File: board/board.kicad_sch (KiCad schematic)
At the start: 35 parts, among them J1 Conn_01x25_Socket, J2 Conn_01x25_Socket, J5 PJ-320B, J6 Screw_Terminal_01x02, J7 Screw_Terminal_01x02, J8 Screw_Terminal_01x02

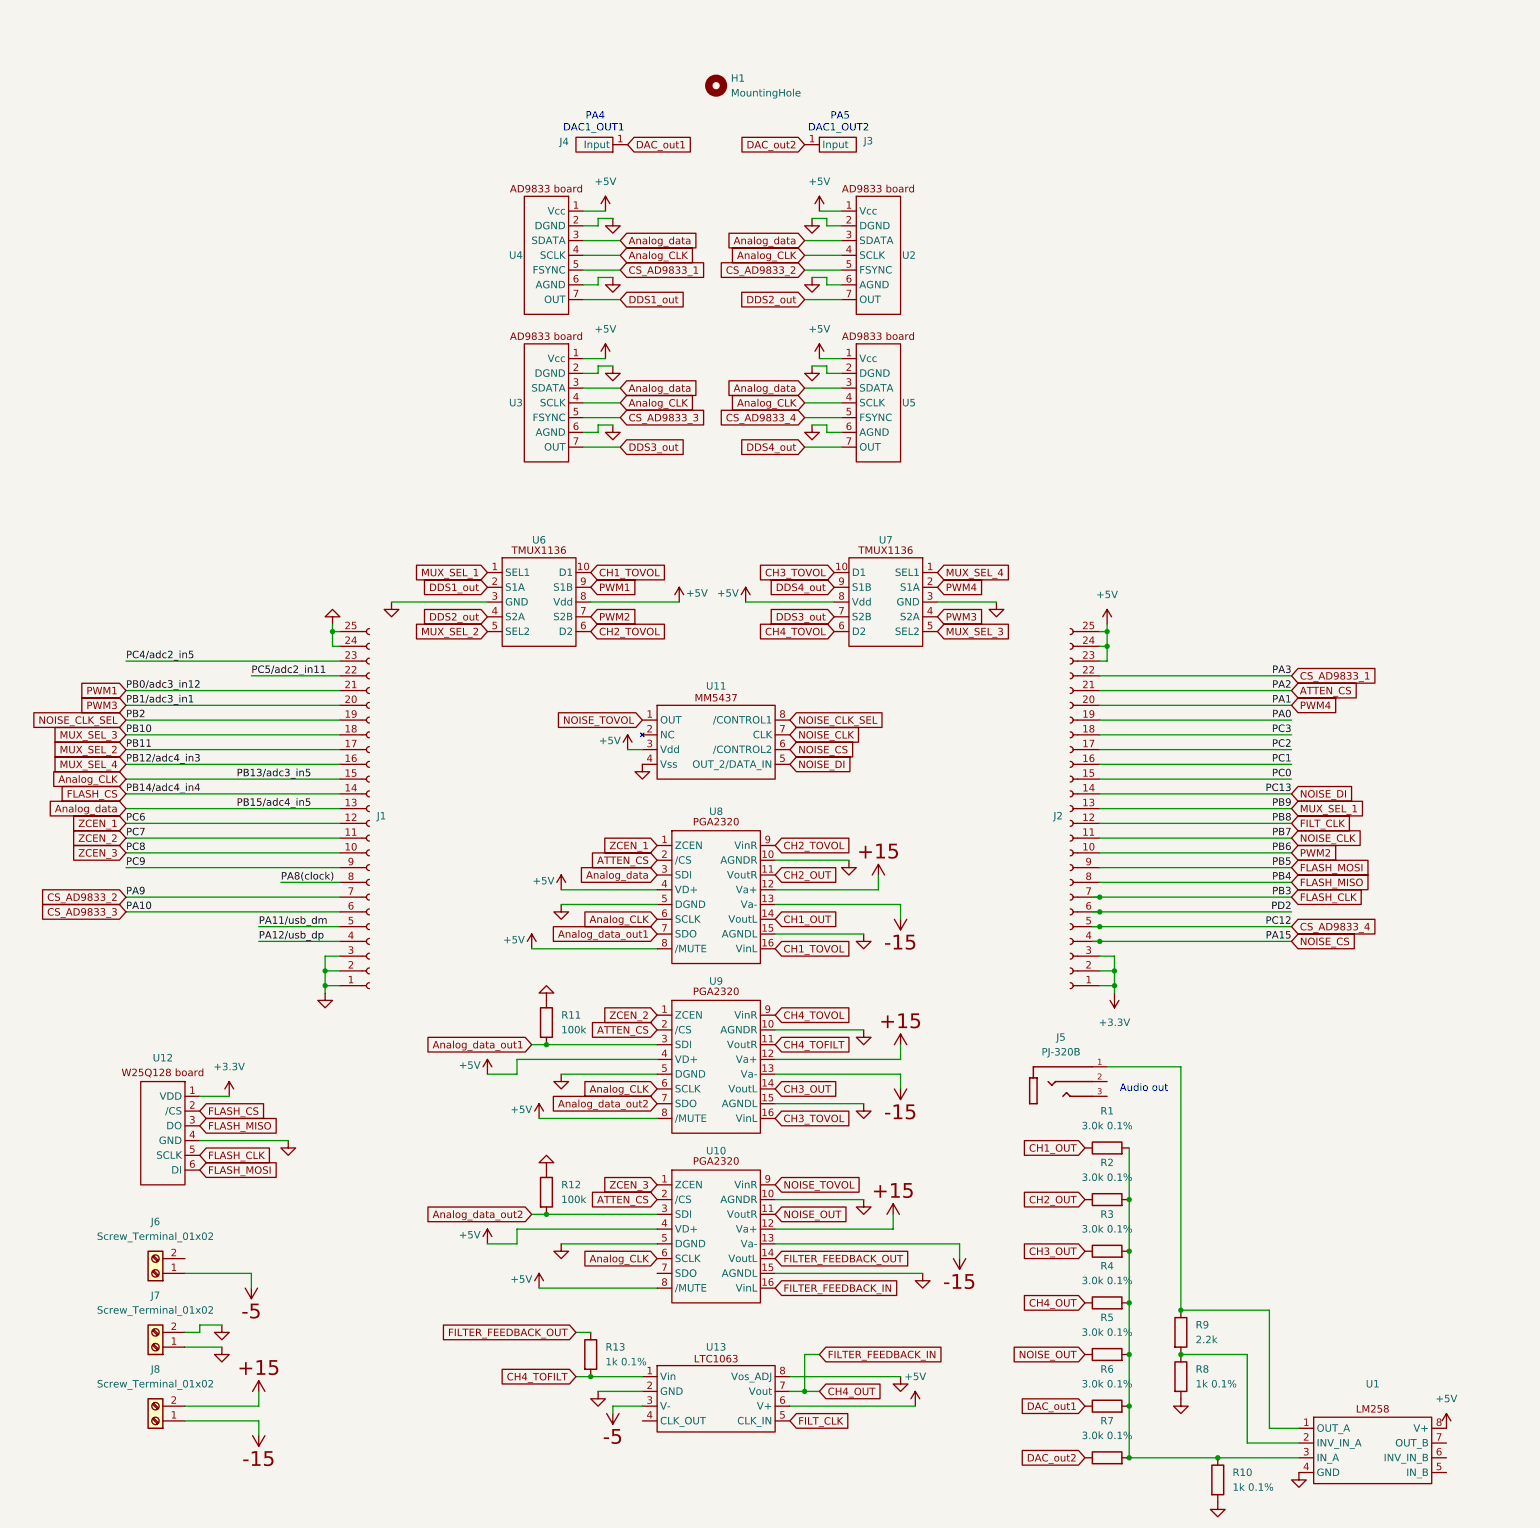
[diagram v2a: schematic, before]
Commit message: fuck it, I ordered 4 2-ch attenuators so let there be DAC volume control!
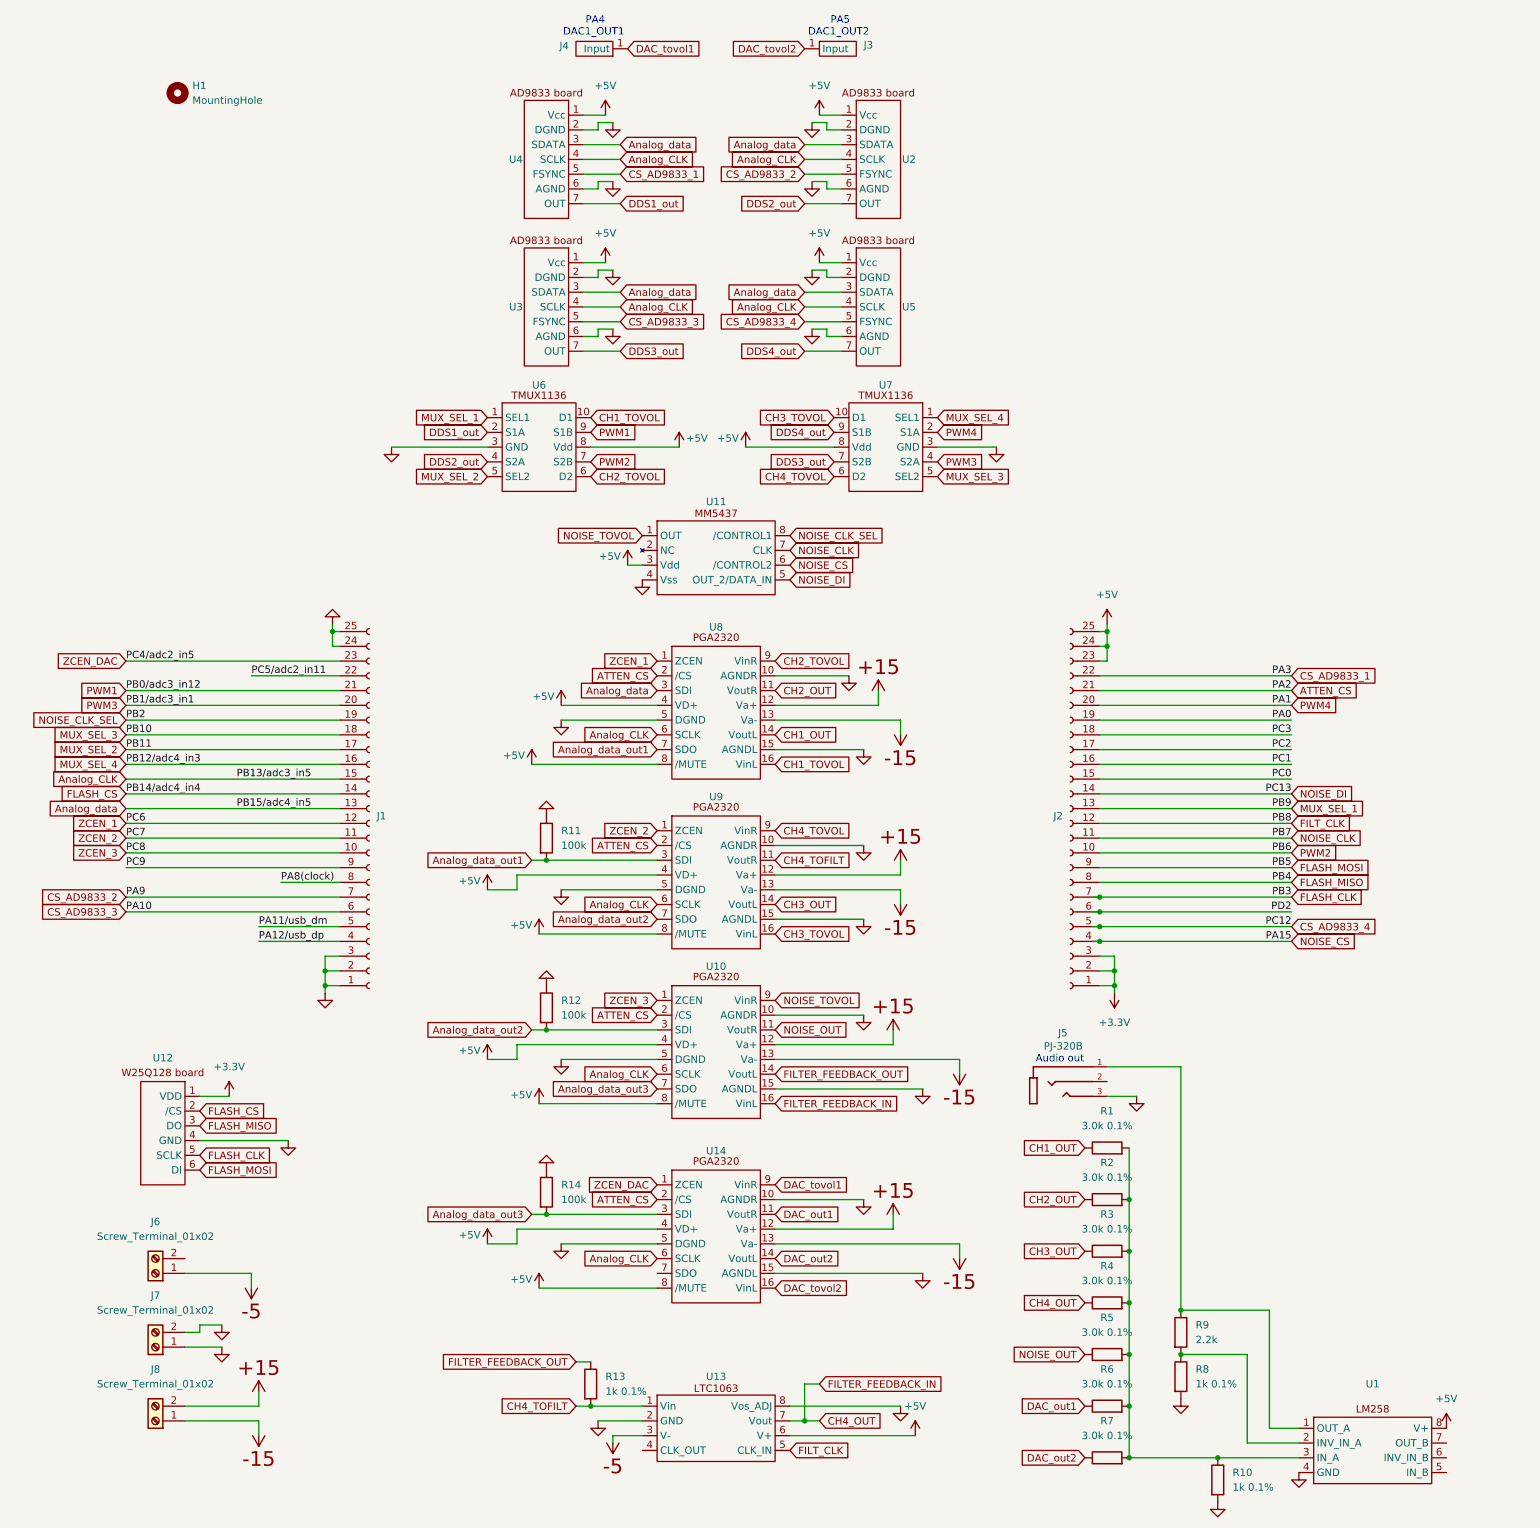
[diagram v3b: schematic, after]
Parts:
- added R14: 100k_0603, 4ms_Resistor:R_0603, symbol 4ms_Resistor:100k_0603
- added U14: ~, Package_SO:SOIC-16W_7.5x10.3mm_P1.27mm, symbol project:PGA2320
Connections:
- net +5V: now also U14.4 (VD+), U14.8 (/MUTE)
- net ATTEN_CS: now also U14.2 (/CS)
- net Analog_CLK: now also U14.6 (SCLK)
- net DAC_out1: now also U14.11 (VoutR); no longer J4.1 (Input)
- net DAC_out2: now also U14.14 (VoutL); no longer J3.1 (Input)
- net GND: now also J5.3, R14.1, U14.10 (AGNDR), U14.15 (AGNDL), U14.5 (DGND)
- net P,+15: now also U14.12 (Va+)
- net P,-15: now also U14.13 (Va-)
- net Analog_data_out3: now reaches U10.7 (SDO)
- net Analog_data_out3: now also R14.2, U14.3 (SDI)
- net PC4/adc2_in5 renamed ZCEN_DAC
- net ZCEN_DAC: now also U14.1 (ZCEN)
- new net DAC_tovol1: J4.1 (Input), U14.9 (VinR)
- new net DAC_tovol2: J3.1 (Input), U14.16 (VinL)
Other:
- moved on the sheet: H1, J3, J4, R11, R12, R13, U10, U11, U13, U2, U3, U4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

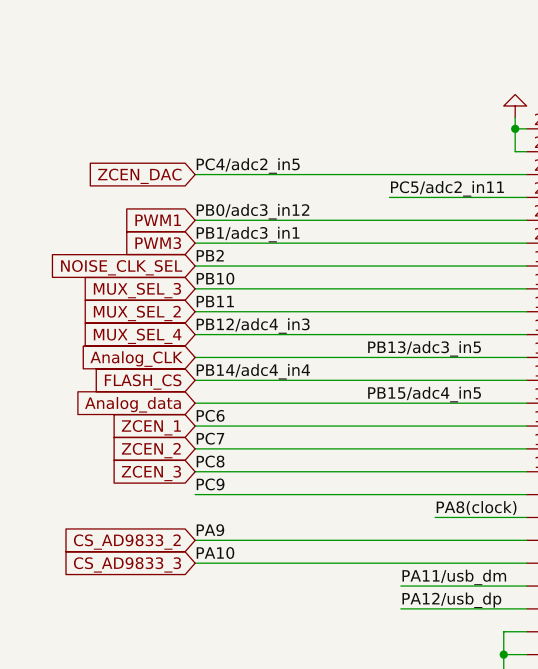
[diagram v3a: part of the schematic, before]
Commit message: free uart pins
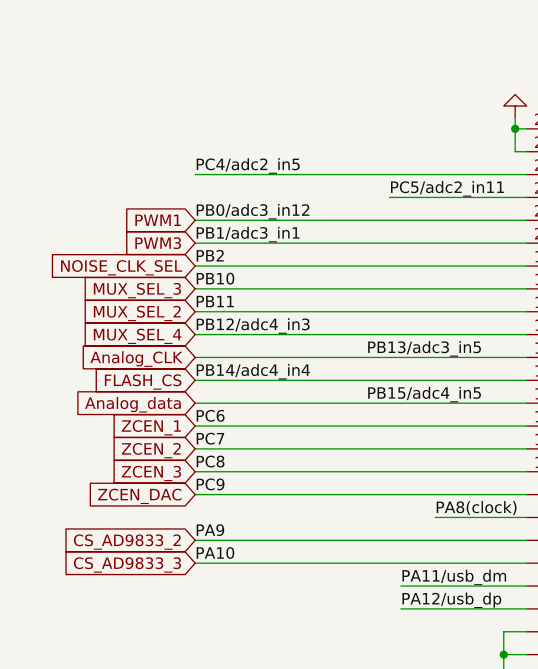
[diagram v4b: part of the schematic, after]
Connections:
- net PC9 is gone; now on net ZCEN_DAC: J1.9 (Pin_9)
- net ZCEN_DAC: no longer J1.23 (Pin_23)
- new net PC4/adc2_in5: J1.23 (Pin_23)
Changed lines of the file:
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@@
+		)
+	)
+	(global_label "ZCEN_DAC"
+		(shape input)
+		(at 48.26 160.02 180)
+		(fields_autoplaced yes)
+		(effects
+			(font
+				(size 1.27 1.27)
+			)
+			(justify right)
+		)
+		(property "Intersheetrefs" "${INTERSHEET_REFS}"
+			(at 35.7196 160.02 0)
+			(effects
+				(font
+					(size 1.27 1.27)
+				)
+				(justify right)
+				(hide yes)
+			)
 		)
 	)
@@
 			(effects
 				(font
-					(size 1.27 1.27)
-				)
-				(justify right)
-				(hide yes)
-			)
-		)
-	)
-	(global_label "ZCEN_DAC"
-		(shape input)
-		(at 48.26 124.46 180)
-		(fields_autoplaced yes)
-		(effects
-			(font
-				(size 1.27 1.27)
-			)
-			(justify right)
-		)
-		(property "Intersheetrefs" "${INTERSHEET_REFS}"
-			(at 35.7196 124.46 0)
-			(effects
-				(font

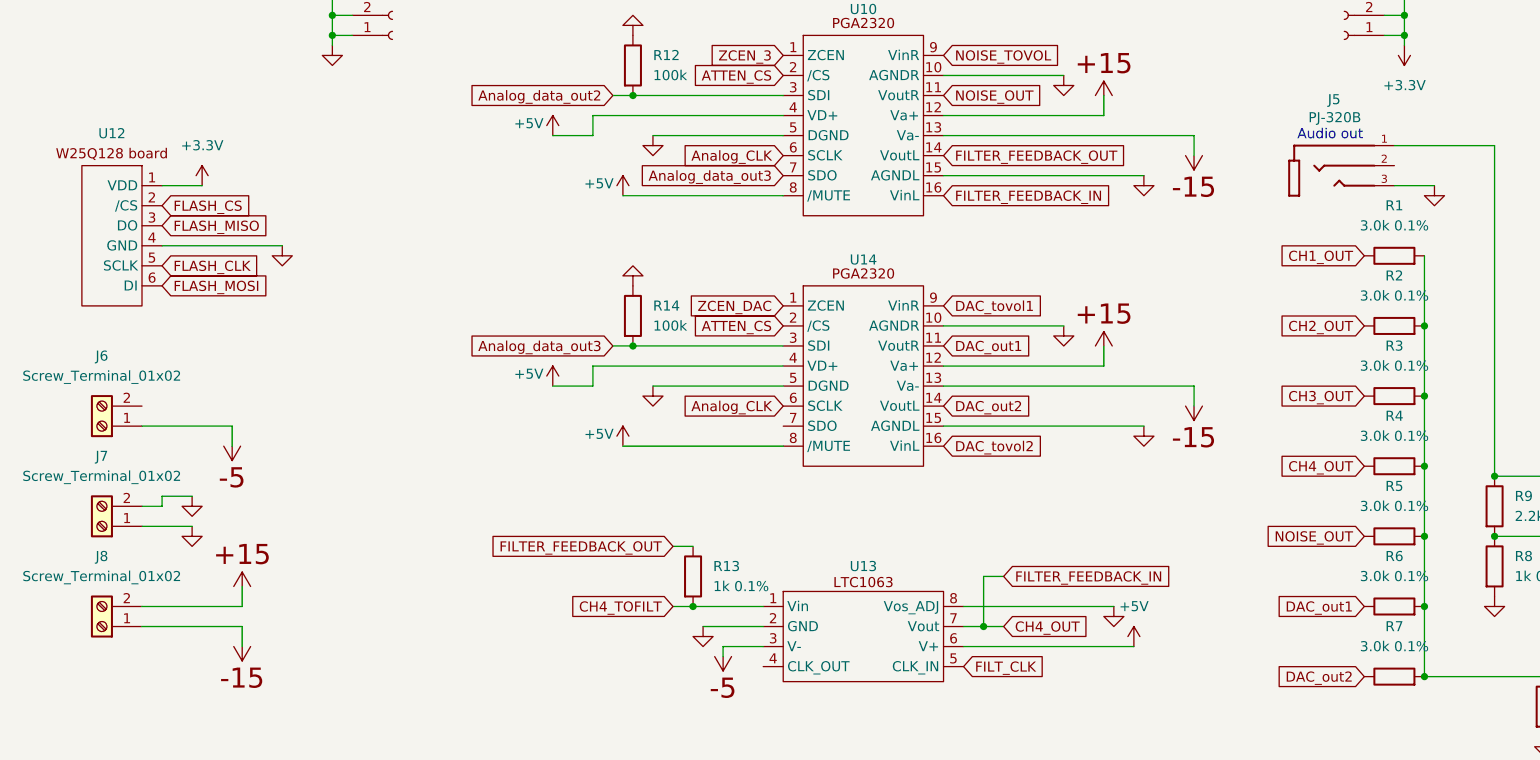
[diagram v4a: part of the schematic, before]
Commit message: added 1 more resistor to filter feedback, added +5v to remaining screw terminal, connected L & R audio channels for 3.5 mm jack
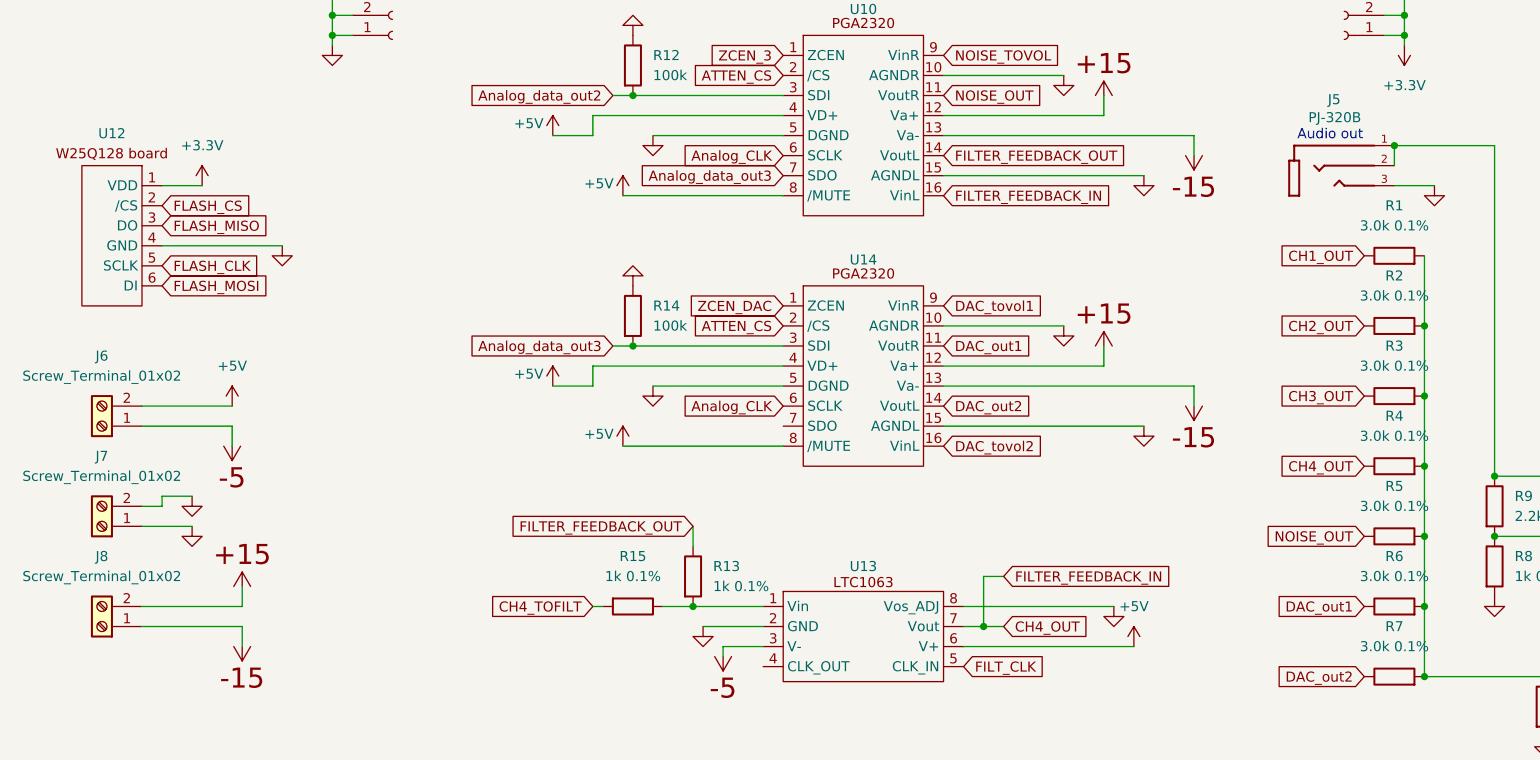
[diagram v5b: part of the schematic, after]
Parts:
- added R15: 1k_0603_0.1%, 4ms_Resistor:R_0603, symbol 4ms_Resistor:1k_0603_0.1%
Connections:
- net +5V: now also J6.2 (Pin_2)
- net CH4_TOFILT: now also R15.2; no longer R13.2, U13.1 (Vin)
- net at J5.1, R9.1, U1.1 (OUT_A): now also J5.2
- new net: R13.2, R15.1, U13.1 (Vin)
